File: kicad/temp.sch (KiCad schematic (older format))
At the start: 46 parts, among them U901 AMC1311B, U902 AMC1311B, U903 ADM2483, U904 AMC1311B, U905 AMC1311B

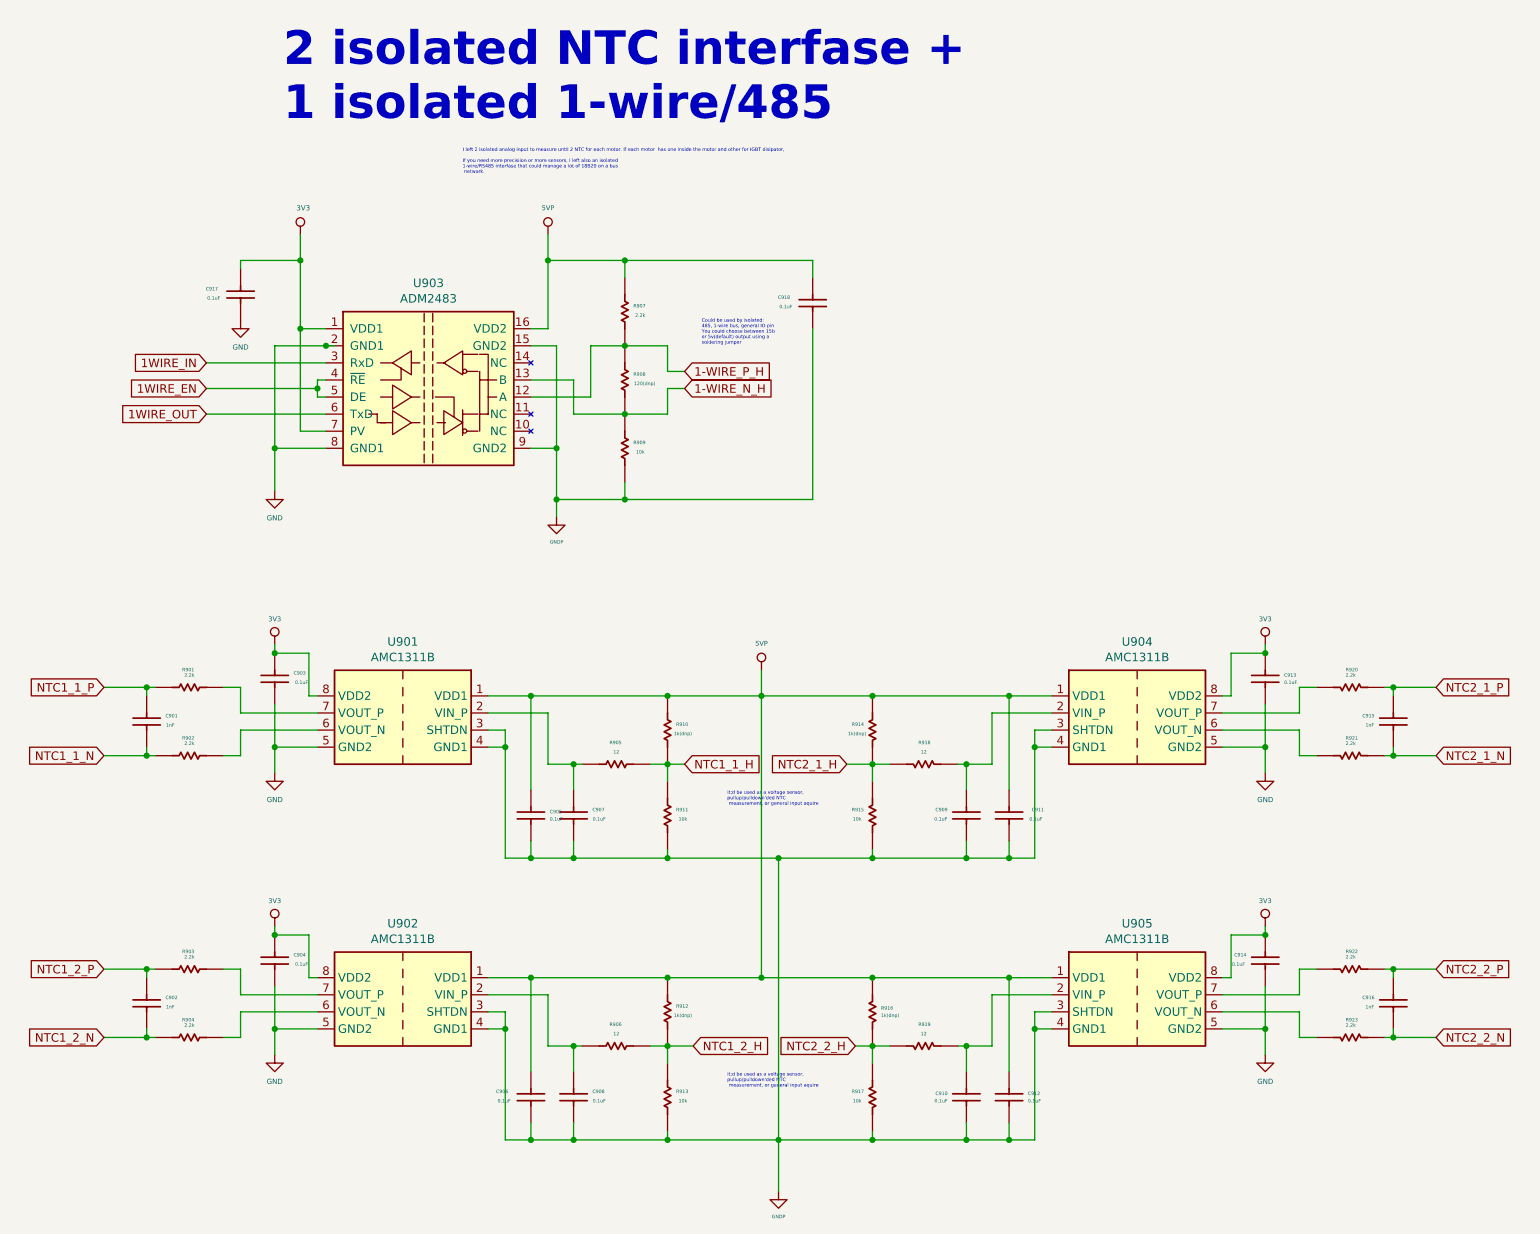
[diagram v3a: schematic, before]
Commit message: changes in footprints
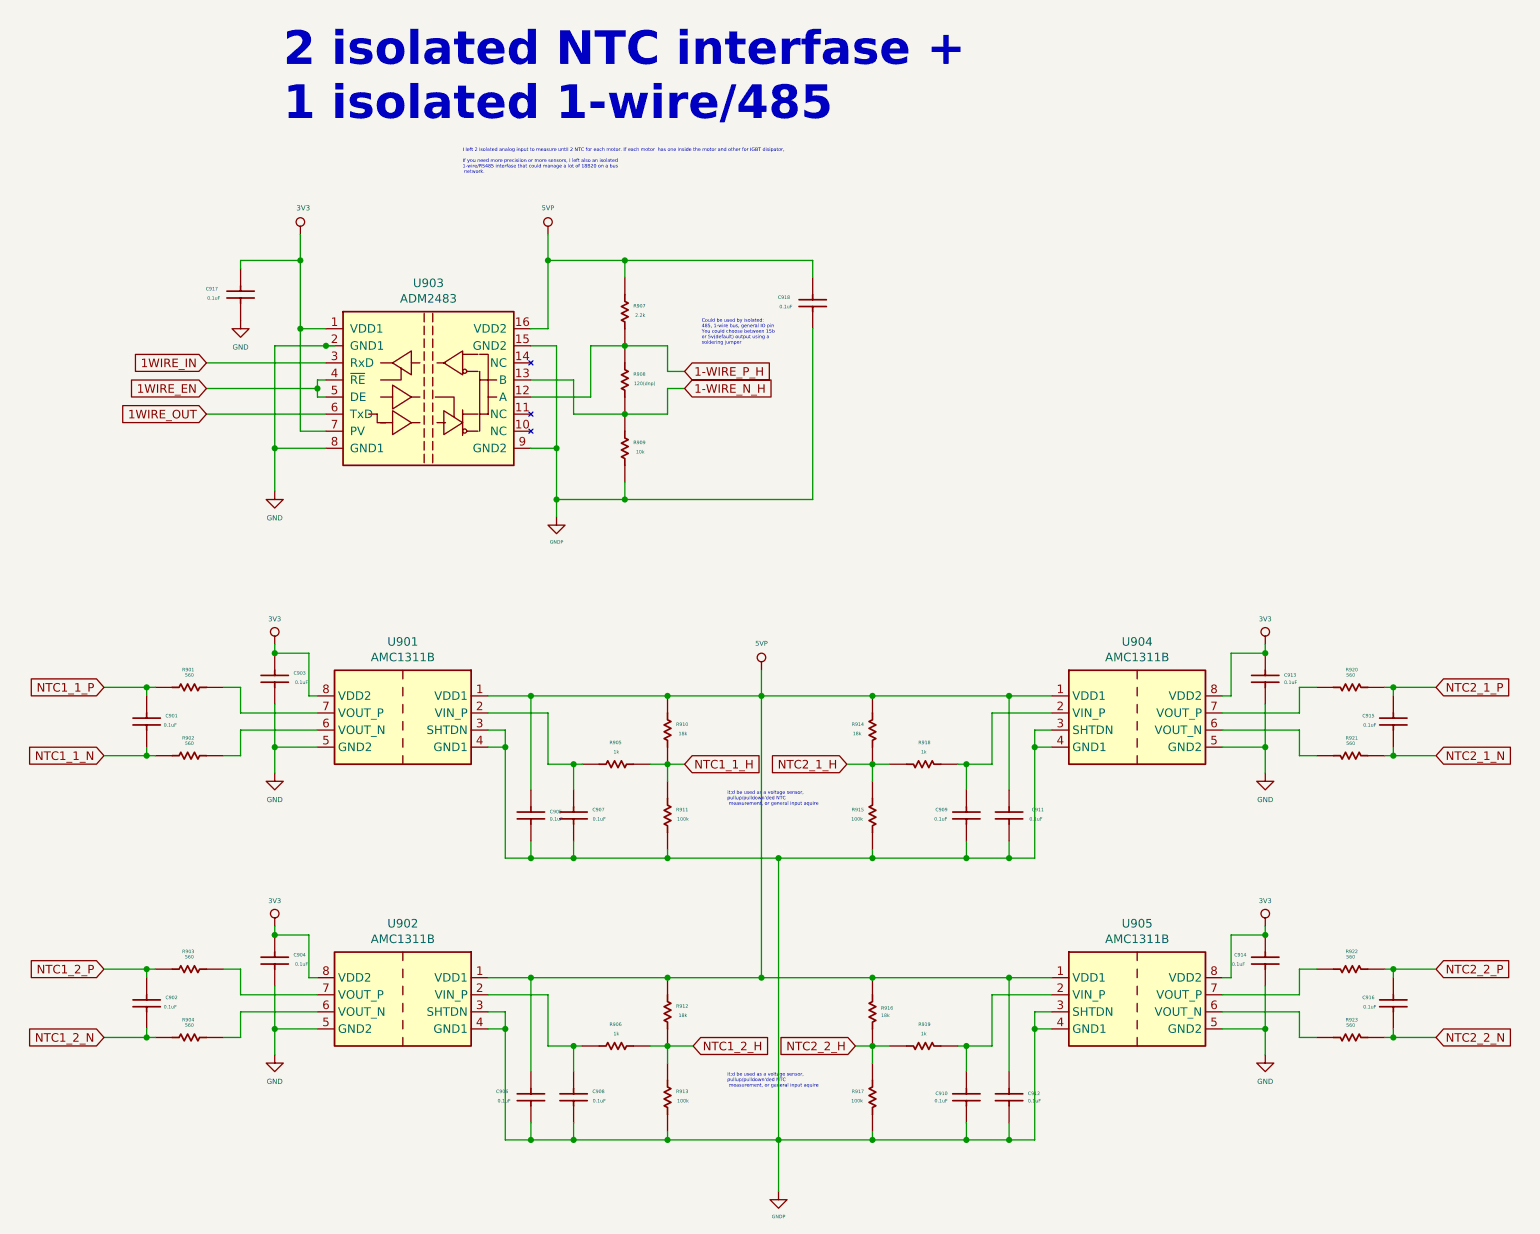
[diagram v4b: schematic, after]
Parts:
- C901, C902, C915, C916: value 1nF -> 0.1uF; Description CAP CER 1000PF 16V X7R 0603 -> CAP CER 0.1UF 16V X7R 0603; PartNumber 0603B102K160CT -> CC0603KPX7R7BB104; digikey 1292-1378-1-ND -> 311-1335-1-ND; price@10 0.04100 -> 0.05800
- R901, R902, R903, R904, R920, R921, R922, R923: value 2.2k -> 560; Description 2.2 kOhms ±5% 0.1W, 1/10W Chip Resistor 0603 (1608 Metric) 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 -> 560 Ohms ±5% 0.1W, 1/10W Chip Resistor 0603 (1608 Metric) M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; PartNumber ERJ-3GEYJ222V -> CR0603-JW-561ELF; digikey P2.2KGCT-ND -> 118-CR0603-JW-561ELFCT-ND; price@10 0.04500 -> 0.02600
- R905, R906, R918, R919: value 12 -> 1k; Description 12 Ohms ±5% 0.1W, 1/10W Chip Resistor 0603 (1608 Metric) Mo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 -> 1 kOhms ±5% 0.1W, 1/10W Chip Resistor 0603 (1608 Metric) Mo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; PartNumber RC0603JR-0712RL -> RC0603JR-071KL; digikey 311-12GRCT-ND -> 311-1.0KGRCT-ND
- R910, R912, R914, R916: value 1k(dnp) -> 18k; Description 1 kOhms ±5% 0.1W, 1/10W Chip Resistor 0603 (1608 Metric) Mo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 -> 18 kOhms ±5% 0.1W, 1/10W Chip Resistor 0603 (1608 Metric) A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; PartNumber RC0603JR-071KL -> RK73B1JTTD183J; digikey 311-1.0KGRCT-ND -> 2019-RK73B1JTTD183JCT-ND
- R911, R913, R915, R917: value 10k -> 100k; Description 10 kOhms ±5% 0.1W, 1/10W Chip Resistor 0603 (1608 Metric) M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 -> 100 kOhms ±5% 0.1W, 1/10W Chip Resistor 0603 (1608 Metric) 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; PartNumber RC0603JR-0710KL -> CR0603-JW-104ELF; digikey 311-10KGRCT-ND -> CR0603-JW-104ELFCT-ND; price@10 0.01900 -> 0.01500

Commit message: fine imprivements
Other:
- note added: "it'd be used as a voltage sensor, \npullup/pulldown'ded NTC\n measurement, or general input aquire"
- note removed: "it;d be used as a voltage sensor, \npullup/pulldown'ded NTC\n measurement, or general input aquire"
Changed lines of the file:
@@
 2 isolated NTC interfase +\n1 isolated 1-wire/485\n
 Text Notes 9600 5300 0    20   ~ 0
-it;d be used as a voltage sensor, \npullup/pulldown'ded NTC\n measurement, or general input aquire
+it'd be used as a voltage sensor, \npullup/pulldown'ded NTC\n measurement, or general input aquire
 Wire Wire Line
 	8450 2600 8600 2600
@@
 	8300 6600 8300 7250
 Text Notes 9600 6950 0    20   ~ 0
-it;d be used as a voltage sensor, \npullup/pulldown'ded NTC\n measurement, or general input aquire
-$Comp
-L servo:Capacitor C?
+it'd be used as a voltage sensor, \npullup/pulldown'ded NTC\n measurement, or general input aquire
+$Comp
+L servo:Capacitor C?

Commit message: gerbers + pnp + bom ready
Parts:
- C901, C902, C903, C904, C905, C906, C907, C908, C909, C910, C911, C912, C913, C914, C915, C916, C917, C918, R901, R902, R903, R904, R905, R906, R907, R908, R909, R910, R911, R912, R913, R914, R915, R916, R917, R918, R919, R920, R921, R922, R923: bom_1 (none) -> 1; bom_2 (none) -> 1; bom_3 (none) -> 1
- U901, U902, U903, U904, U905: bom_2 (none) -> 1; bom_3 (none) -> 1

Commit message: some details on gerbers, now released
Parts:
- U901, U902, U903, U904, U905: bom_1 (none) -> 0
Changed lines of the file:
@@
 F 6 "ADM2483BRWZ-ND" H 0   0   50  0001 C CNN "digikey"
 F 7 "5.59000" H 0   0   50  0001 C CNN "price@10"
-F 8 "" H 0   0   50  0001 C CNN "bom_1"
+F 8 "0" H 0   0   50  0001 C CNN "bom_1"
 F 9 "1" H 0   0   50  0001 C CNN "bom_2"
 F 10 "1" H 0   0   50  0001 C CNN "bom_3"
@@
 F 6 "296-47610-ND" H 0   0   50  0001 C CNN "digikey"
 F 7 "7.24300" H 0   0   50  0001 C CNN "price@10"
-F 8 "" H 0   0   50  0001 C CNN "bom_1"
+F 8 "0" H 0   0   50  0001 C CNN "bom_1"
 F 9 "1" H 0   0   50  0001 C CNN "bom_2"
 F 10 "1" H 0   0   50  0001 C CNN "bom_3"
@@
 F 6 "296-47610-ND" H 0   0   50  0001 C CNN "digikey"
 F 7 "7.24300" H 0   0   50  0001 C CNN "price@10"
-F 8 "" H 0   0   50  0001 C CNN "bom_1"
+F 8 "0" H 0   0   50  0001 C CNN "bom_1"
 F 9 "1" H 0   0   50  0001 C CNN "bom_2"
 F 10 "1" H 0   0   50  0001 C CNN "bom_3"
@@
 F 6 "296-47610-ND" H 0   0   50  0001 C CNN "digikey"
 F 7 "7.24300" H 0   0   50  0001 C CNN "price@10"
-F 8 "" H 0   0   50  0001 C CNN "bom_1"
+F 8 "0" H 0   0   50  0001 C CNN "bom_1"
 F 9 "1" H 0   0   50  0001 C CNN "bom_2"
 F 10 "1" H 0   0   50  0001 C CNN "bom_3"
@@
 F 6 "296-47610-ND" H 0   0   50  0001 C CNN "digikey"
 F 7 "7.24300" H 0   0   50  0001 C CNN "price@10"
-F 8 "" H 0   0   50  0001 C CNN "bom_1"
-F 9 "1" H 0   0   50  0001 C CNN "bom_2"
-F 10 "1" H 0   0   50  0001 C CNN "bom_3"
+F 8 "0" H 0   0   50  0001 C CNN "bom_1"
+F 9 "1" H 0   0   50  0001 C CNN "bom_2"
+F 10 "1" H 0   0   50  0001 C CNN "bom_3"
